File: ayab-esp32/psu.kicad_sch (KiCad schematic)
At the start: 47 parts, among them J602 Brother_5P, J604 Brother_4R, Q601 LP9435LT1G, U401 XL1509, U402 XL1509

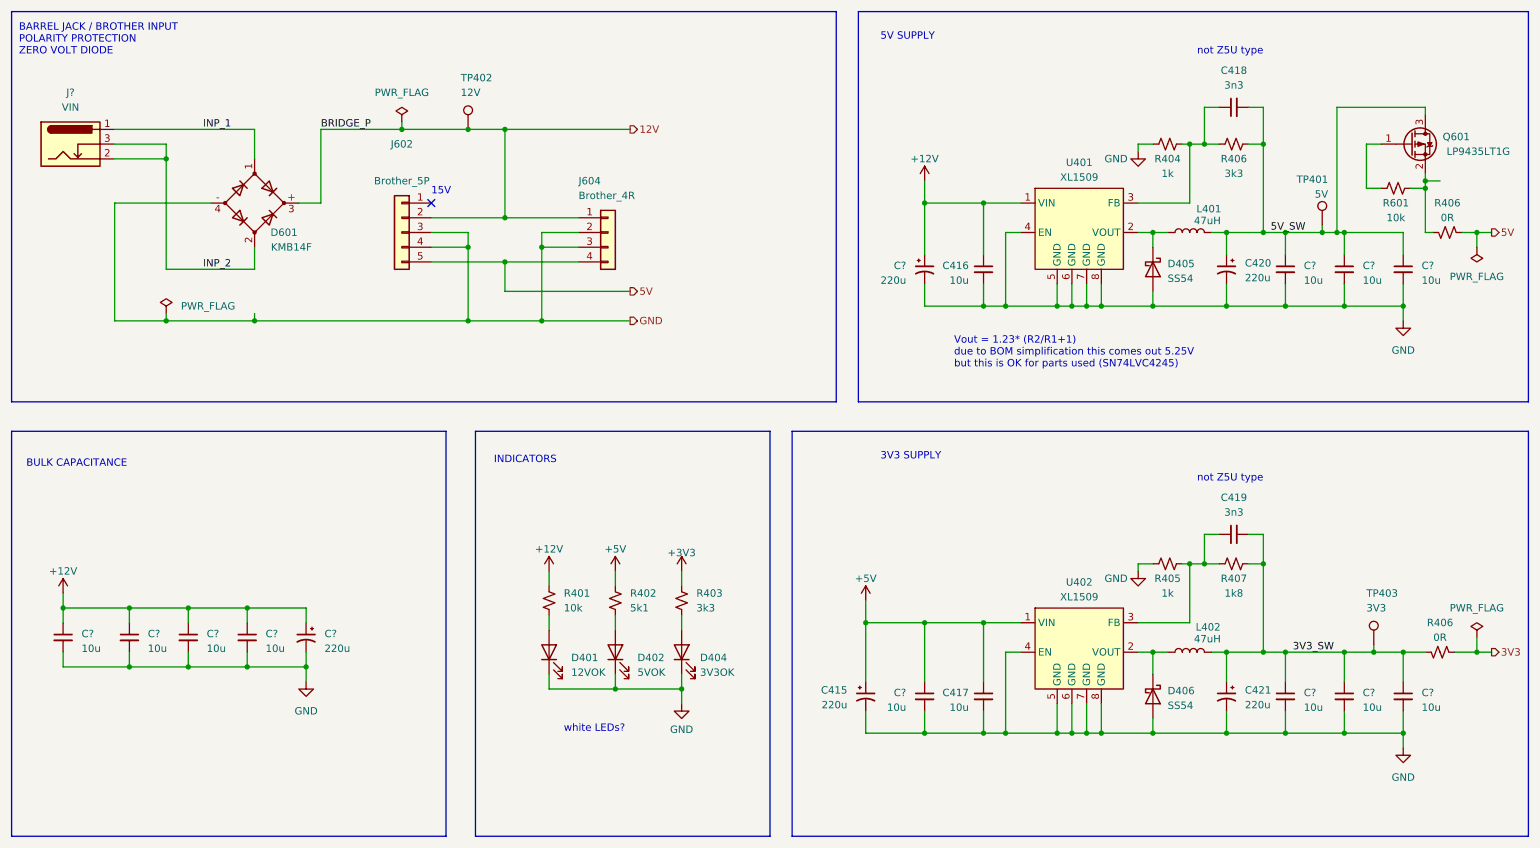
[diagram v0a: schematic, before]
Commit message: clean ERC DRC, fix library paths
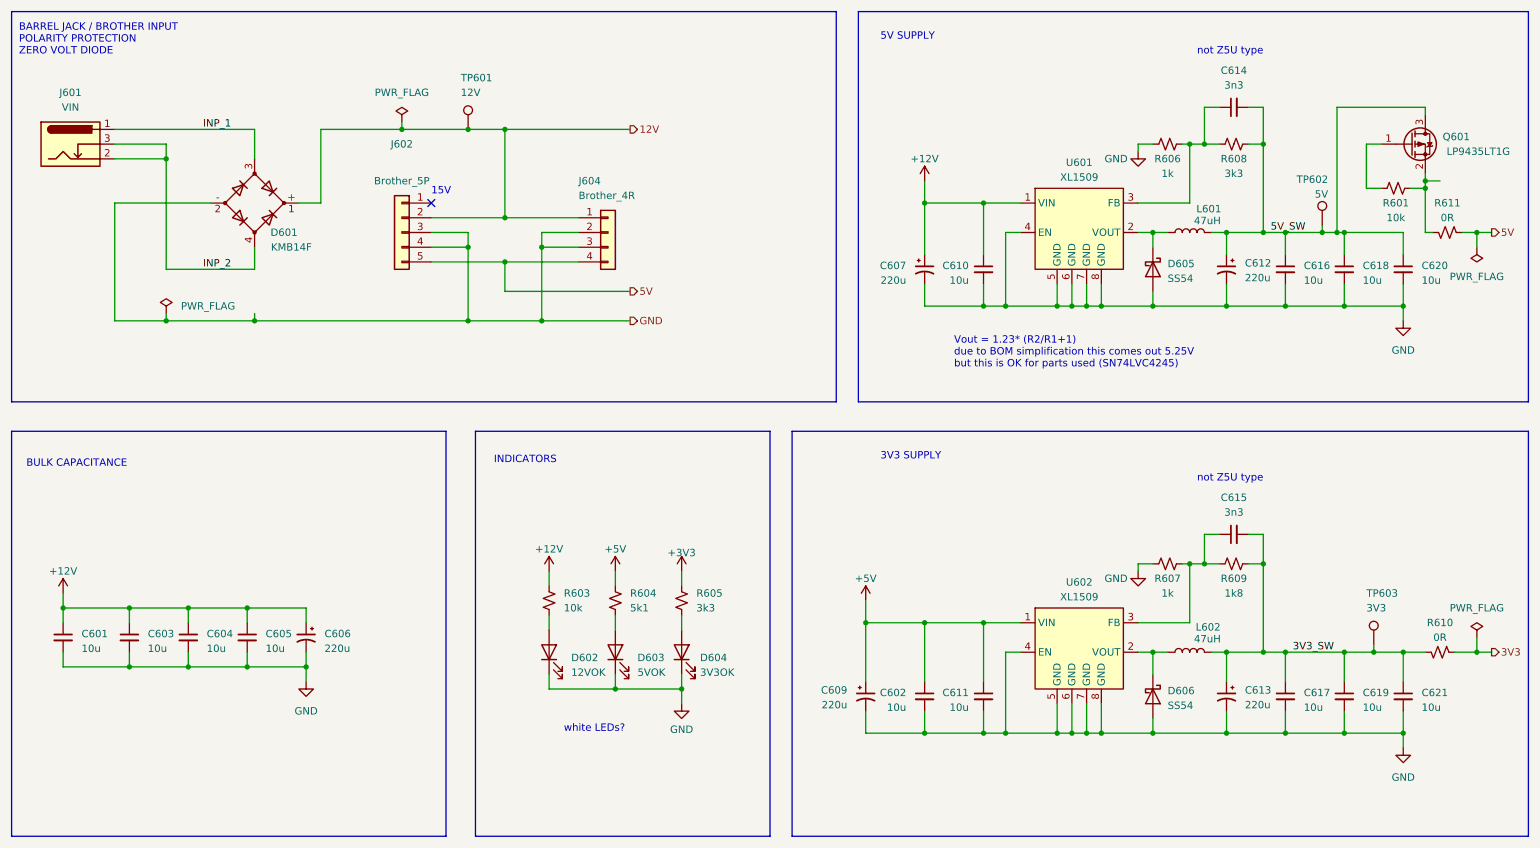
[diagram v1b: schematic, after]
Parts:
- D601: footprint easyeda2kicad:MBF-SMD_L4.8-W3.8-P2.54-LS6.8-TL -> Library:MBF-SMD_L4.8-W3.8-P2.54-LS6.8-TL
- J601: renamed from J?; footprint easyeda2kicad:DC-IN-TH_DC-005-5A-2.0-SMT -> Library:DC-IN-TH_DC-005-5A-2.0-SMT
- gave numbers to parts that had none: 13
- renumbered C415 to C609, C416 to C610, C417 to C611, C420 to C612, C421 to C613, C418 to C614, C419 to C615, D401 to D602, D402 to D603, D404 to D604, D405 to D605, D406 to D606, L401 to L601, L402 to L602, R401 to R603, R402 to R604, R403 to R605, R404 to R606, R405 to R607, R406 to R608, R407 to R609, R406 to R610, R406 to R611, TP402 to TP601, TP401 to TP602, TP403 to TP603, U401 to U601, U402 to U602
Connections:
- net 12V: now also D601.1 (+); no longer D601.3 (+)
- net GND: now also D601.2 (-); no longer D601.4 (-)
- net INP_1: now also D601.3; no longer D601.1
- net INP_2: now also D601.4; no longer D601.2
